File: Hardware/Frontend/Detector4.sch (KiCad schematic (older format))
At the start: 27 parts, among them J6 Conn_Coaxial, U10 OPA145ID, U11 OPA145ID, U12 OPA145ID

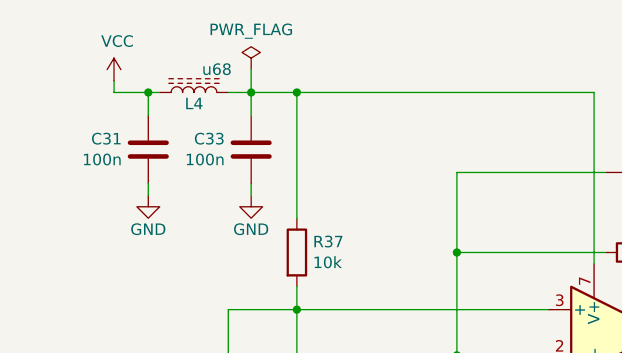
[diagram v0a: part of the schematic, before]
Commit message: add bom
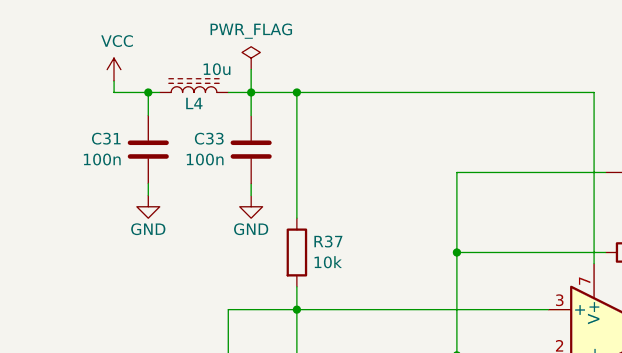
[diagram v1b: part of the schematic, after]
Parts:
- L4: value u68 -> 10u
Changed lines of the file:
@@
 AR Path="/6126CBD6/614305B5" Ref="L4"  Part="1"
 F 0 "L4" V 2800 2000 50  0000 C CNN
-F 1 "u68" V 2950 2100 50  0000 C CNN
+F 1 "10u" V 2950 2100 50  0000 C CNN
 F 2 "Inductor_SMD:L_0805_2012Metric" H 2850 2000 50  0001 C CNN
 F 3 "" H 2850 2000 50  0001 C CNN
